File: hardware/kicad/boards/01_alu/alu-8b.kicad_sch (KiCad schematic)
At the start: 16 parts

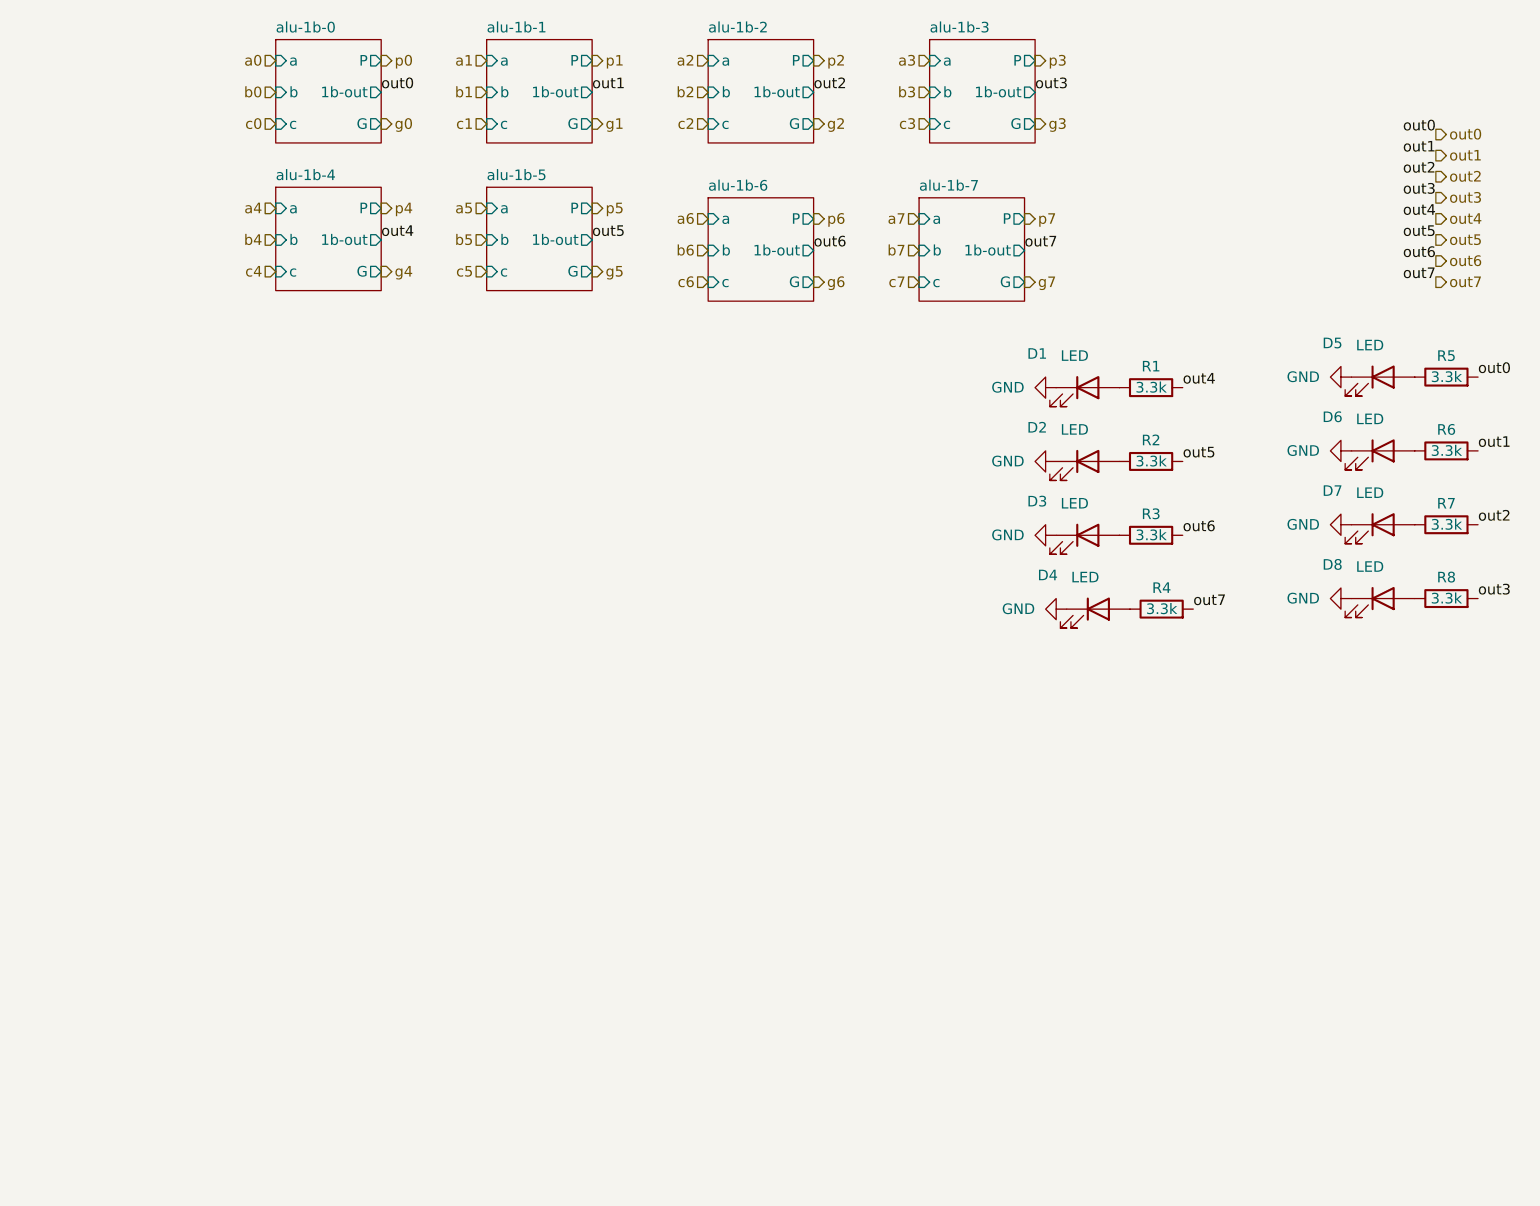
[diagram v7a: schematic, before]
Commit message: refactor: placing buses in design across alu to improve readability and debugging
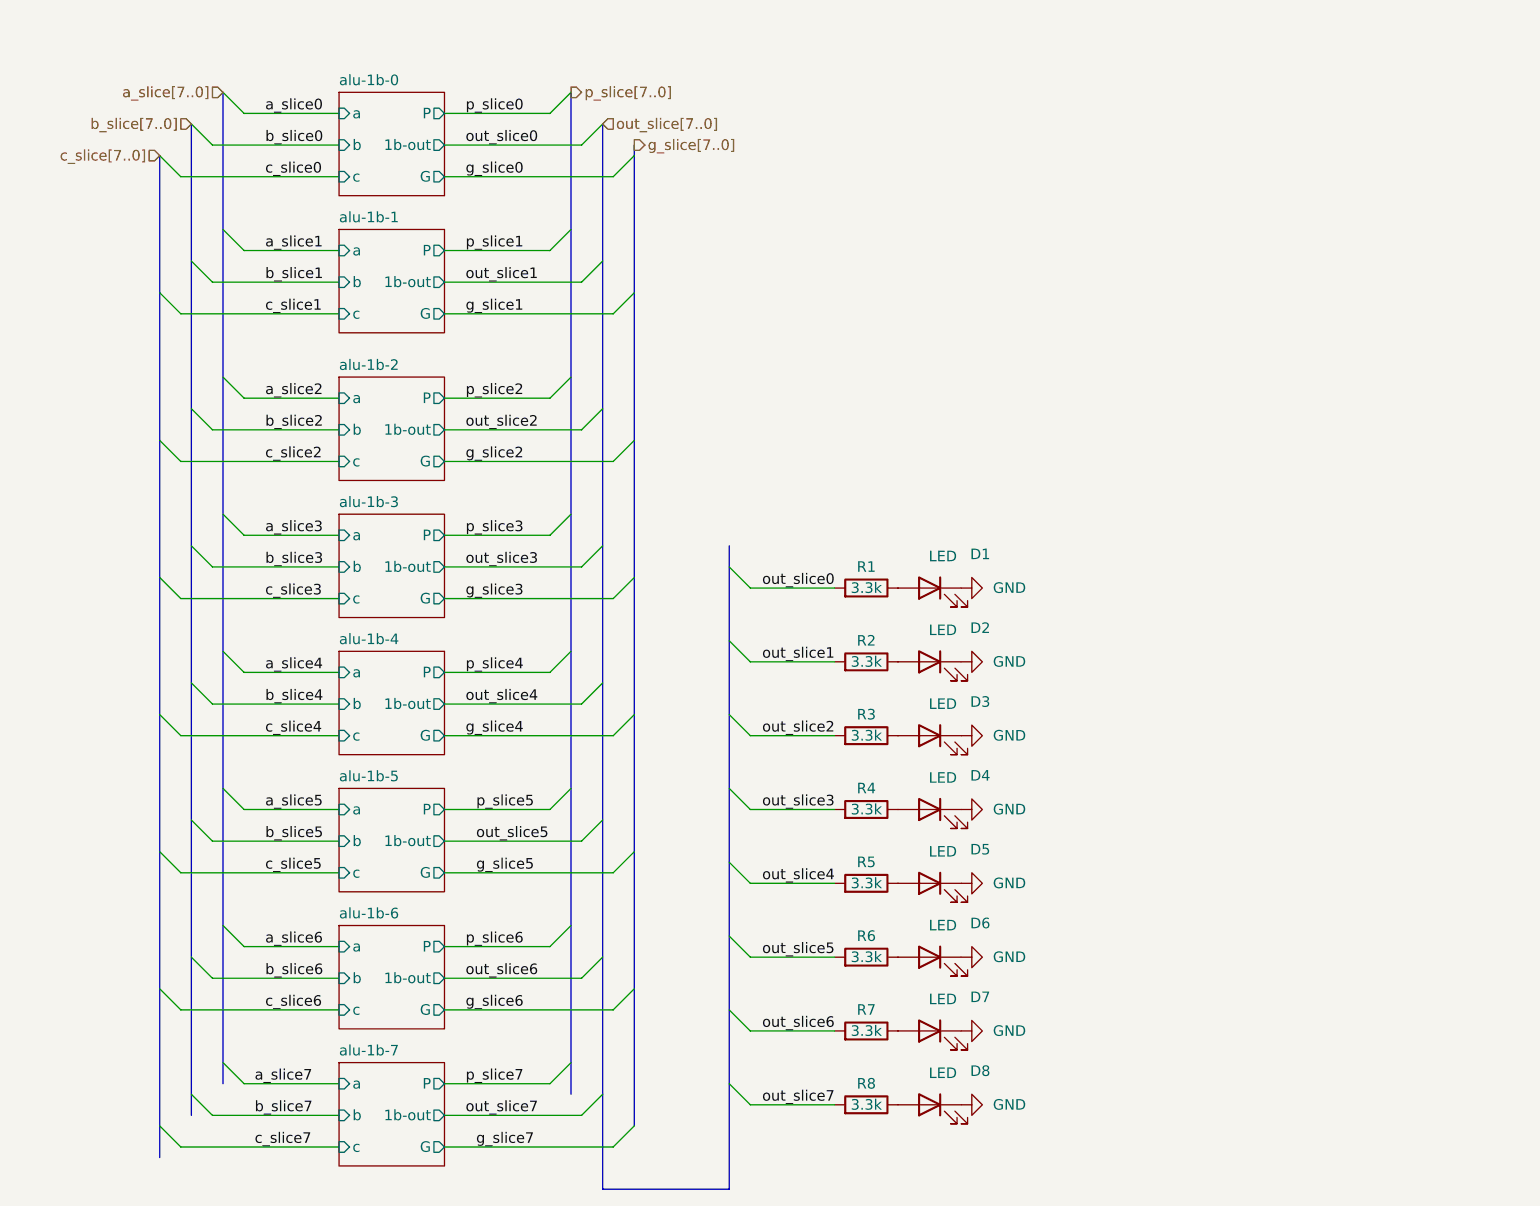
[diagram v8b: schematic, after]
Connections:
- net out0 renamed out_slice4
- net out1 renamed out_slice5
- net out2 renamed out_slice6
- net out3 renamed out_slice7
- net out4 renamed out_slice0
- net out5 renamed out_slice1
- net out6 renamed out_slice2
- net out7 renamed out_slice3
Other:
- moved on the sheet: D1, R1
